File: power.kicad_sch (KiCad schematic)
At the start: 29 parts, among them J7 Conn_01x02, Q1 CSD17311Q5, Q2 CSD17311Q5, U10 DS4432U+, U8 INA260, U9 TPS40305

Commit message: cleanup
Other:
- title: le bitaxeUltra -> BM1366 bitaxe
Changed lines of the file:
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@@
   (paper "A")
   (title_block
-    (title "le bitaxeUltra")
-    (date "2023-07-10")
-    (rev "0")
+    (title "BM1366 bitaxe")
+    (date "2023-10-10")
+    (rev "1.1")
   )
   (junction (at 135.89 116.84) (diameter 0) (color 0 0 0 0)

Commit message: added missing part numbers. updated BOM and iBOM
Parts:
- J7: now left out of the parts list
- U8: DK 296-47777-1-ND -> 296-45218-5-ND; PARTNO INA260AIPWR -> INA260AIPW
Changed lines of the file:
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@@
       (effects (font (size 1.27 1.27)) hide)
     )
-    (property "PARTNO" "INA260AIPWR" (at 67.945 135.89 0)
-      (effects (font (size 1.27 1.27)) hide)
-    )
-    (property "DK" "296-47777-1-ND" (at 67.945 135.89 0)
+    (property "PARTNO" "INA260AIPW" (at 67.945 135.89 0)
+      (effects (font (size 1.27 1.27)) hide)
+    )
+    (property "DK" "296-45218-5-ND" (at 67.945 135.89 0)
       (effects (font (size 1.27 1.27)) hide)
     )
@@
   )
   (symbol (lib_id "Connector_Generic:Conn_01x02") (at 54.102 91.186 0) (unit 1)
-    (in_bom yes) (on_board yes) (dnp no) (fields_autoplaced)
+    (in_bom no) (on_board yes) (dnp no) (fields_autoplaced)
     (property "Reference" "J7" (at 57.15 92.4559 0)
       (effects (font (size 1.27 1.27)) (justify left))

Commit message: adding gerbers
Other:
- note added: "The INA260 is tricky to source. INA260AIPW and INA260AIPWR are both fine. This part is totally optional, feel free to leave it out if you can't source it. If you DNP it, close J7"
- note removed: "The INA260 is currently out of stock everywhere. This part is totally optional, feel free to leave it out if you can't source it. If you DNP it, close J7"
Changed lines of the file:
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@@
     (effects (font (size 1.27 1.27)) (justify left bottom))
   )
-  (text "The INA260 is currently out of stock everywhere.\nThis part is totally optional, feel free to leave \nit out if you can't source it. If you DNP it, close J7"
+  (text "The INA260 is tricky to source. INA260AIPW and INA260AIPWR are both fine.\nThis part is totally optional, feel free to leave \nit out if you can't source it. If you DNP it, close J7"
     (at 45.085 167.005 0)
     (effects (font (size 1.27 1.27)) (justify left bottom))

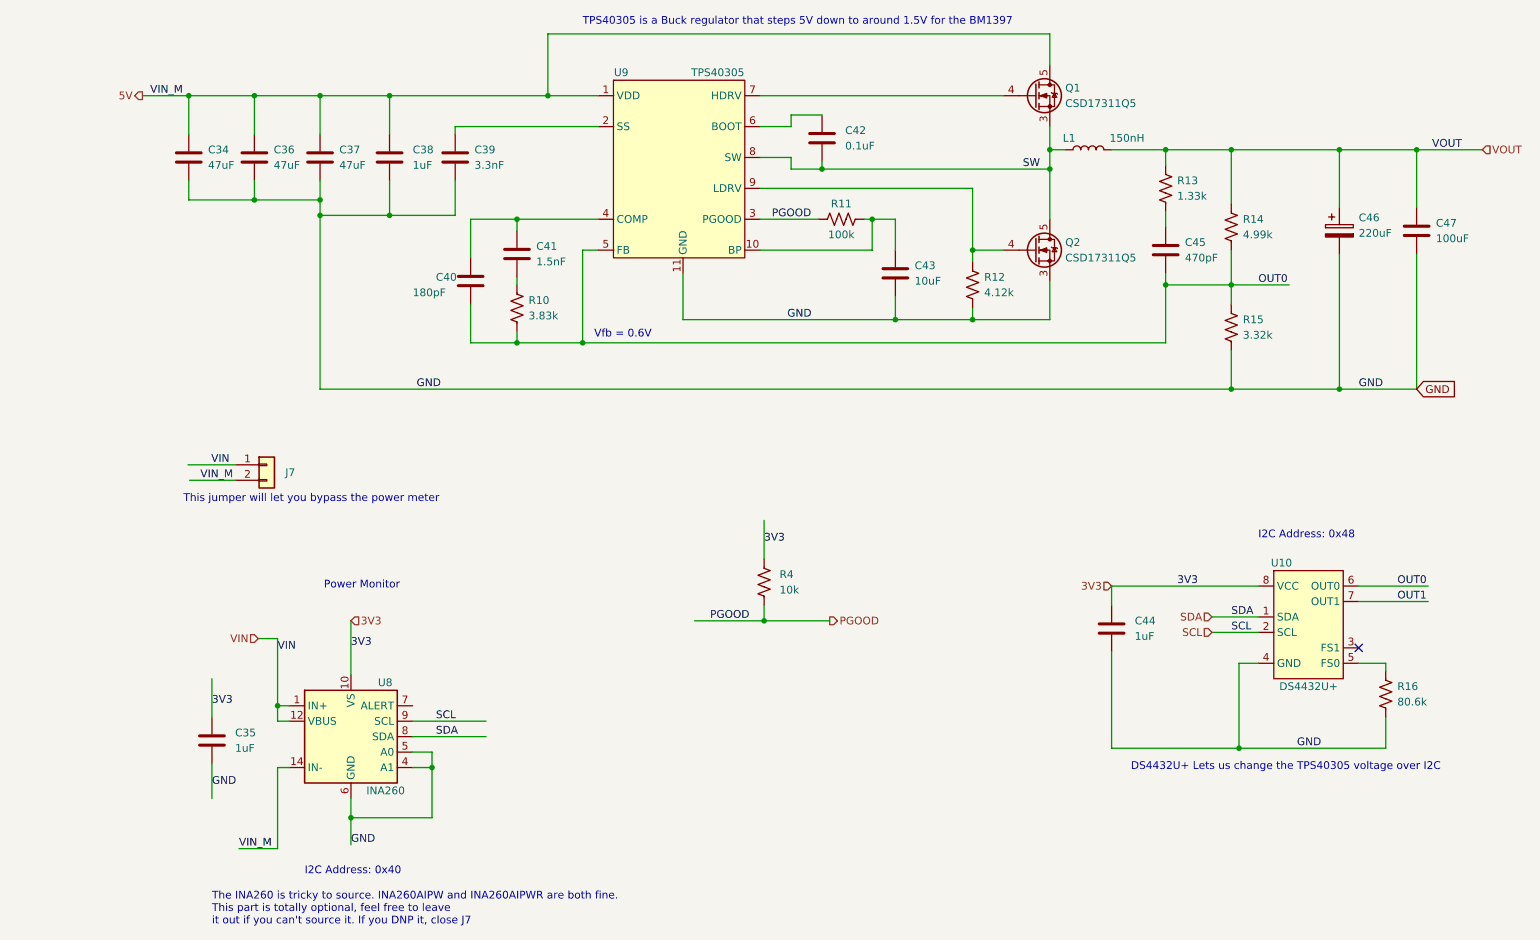
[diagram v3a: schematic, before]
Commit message: added PWR_EN signal to shutdown the TPS40305
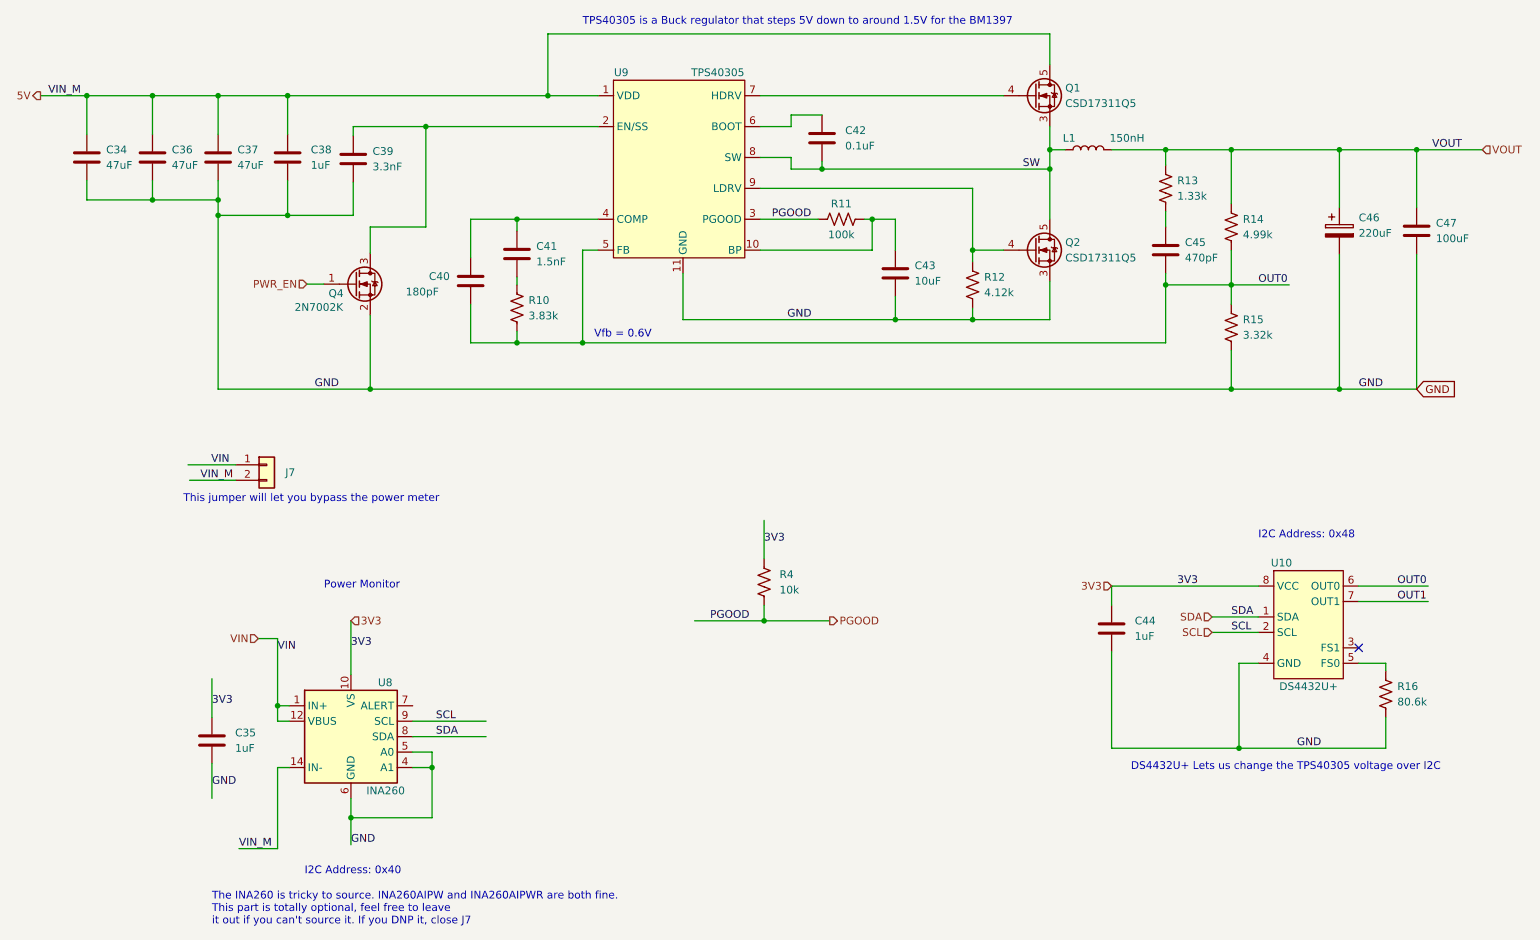
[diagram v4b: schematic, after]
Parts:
- added Q4: 2N7002K, Package_TO_SOT_SMD:SOT-323_SC-70, symbol Transistor_FET:2N7002K
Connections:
- net GND: now also Q4.2 (S)
- net at C39.1, U9.2 (EN/SS): now also Q4.3 (D)
- new net PWR_EN: Q4.1 (G)
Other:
- moved on the sheet: C34, C36, C37, C38, C39

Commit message: misc
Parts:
- R11: now not fitted
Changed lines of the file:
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@@
   )
   (symbol (lib_id "Device:R_US") (at 148.59 50.8 90) (unit 1)
-    (in_bom yes) (on_board yes) (dnp no)
+    (in_bom yes) (on_board yes) (dnp yes)
     (property "Reference" "R11" (at 148.59 48.26 90)
       (effects (font (size 1.27 1.27)))

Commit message: no message
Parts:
- removed R11: 100k, Resistor_SMD:R_0402_1005Metric, symbol Device:R_US
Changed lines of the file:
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@@
   (junction (at 46.101 47.625) (diameter 0) (color 0 0 0 0)
-  )
-  (junction (at 153.67 50.8) (diameter 0) (color 0 0 0 0)
   )
   (junction (at 213.995 137.795) (diameter 0) (color 0 0 0 0)
@@
     (stroke (width 0) (type default))
   )
-  (wire (pts (xy 153.67 55.88) (xy 153.67 50.8))
-    (stroke (width 0) (type default))
-  )
   (wire (pts (xy 230.505 39.37) (xy 230.505 48.895))
     (stroke (width 0) (type default))
@@
     (stroke (width 0) (type default))
   )
-  (wire (pts (xy 135.255 55.88) (xy 153.67 55.88))
+  (wire (pts (xy 135.255 55.88) (xy 157.48 55.88))
     (stroke (width 0) (type default))
   )
@@
     (stroke (width 0) (type default))
   )
-  (wire (pts (xy 152.4 50.8) (xy 153.67 50.8))
-    (stroke (width 0) (type default))
-  )
   (wire (pts (xy 35.306 30.48) (xy 46.101 30.48))
     (stroke (width 0) (type default))
@@
     (stroke (width 0) (type default))
   )
-  (wire (pts (xy 157.48 50.8) (xy 157.48 55.88))
-    (stroke (width 0) (type default))
-  )
   (wire (pts (xy 35.306 30.48) (xy 35.306 36.83))
     (stroke (width 0) (type default))
@@
   )
   (wire (pts (xy 201.93 39.37) (xy 212.725 39.37))
-    (stroke (width 0) (type default))
-  )
-  (wire (pts (xy 153.67 50.8) (xy 157.48 50.8))
     (stroke (width 0) (type default))
   )
@@
     (pin "2")
     (instances
-      (project "bitaxeUltra"
+      (project "bitaxe_RGZ_204_MOD_C"
         (path "/e63e39d7-6ac0-4ffd-8aa3-1841a4541b55/8ec0a9c6-2b78-44ef-a83d-9047d2828409"
           (reference "C43") (unit 1)
@@
     (pin "2")
     (instances
-      (project "bitaxeUltra"
+      (project "bitaxe_RGZ_204_MOD_C"
         (path "/e63e39d7-6ac0-4ffd-8aa3-1841a4541b55/8ec0a9c6-2b78-44ef-a83d-9047d2828409"
           (reference "R14") (unit 1)
@@
     (pin "2")
     (instances
-      (project "bitaxeUltra"
+      (project "bitaxe_RGZ_204_MOD_C"
         (path "/e63e39d7-6ac0-4ffd-8aa3-1841a4541b55/8ec0a9c6-2b78-44ef-a83d-9047d2828409"
           (reference "C37") (unit 1)
@@
     (pin "2")
     (instances
-      (project "bitaxeUltra"
+      (project "bitaxe_RGZ_204_MOD_C"
         (path "/e63e39d7-6ac0-4ffd-8aa3-1841a4541b55/8ec0a9c6-2b78-44ef-a83d-9047d2828409"
           (reference "C46") (unit 1)
@@
     (pin "9")
     (instances
-      (project "bitaxeUltra"
+      (project "bitaxe_RGZ_204_MOD_C"
         (path "/e63e39d7-6ac0-4ffd-8aa3-1841a4541b55/8ec0a9c6-2b78-44ef-a83d-9047d2828409"
           (reference "U9") (unit 1)
@@
     (pin "9")
     (instances
-      (project "bitaxeUltra"
+      (project "bitaxe_RGZ_204_MOD_C"
         (path "/e63e39d7-6ac0-4ffd-8aa3-1841a4541b55/8ec0a9c6-2b78-44ef-a83d-9047d2828409"
           (reference "U8") (unit 1)
@@
     (pin "2")
     (instances
-      (project "bitaxeUltra"
+      (project "bitaxe_RGZ_204_MOD_C"
         (path "/e63e39d7-6ac0-4ffd-8aa3-1841a4541b55/8ec0a9c6-2b78-44ef-a83d-9047d2828409"
           (reference "C34") (unit 1)
@@
     (pin "5")
     (instances
-      (project "bitaxeUltra"
+      (project "bitaxe_RGZ_204_MOD_C"
         (path "/e63e39d7-6ac0-4ffd-8aa3-1841a4541b55/8ec0a9c6-2b78-44ef-a83d-9047d2828409"
           (reference "Q2") (unit 1)
@@
     (pin "2")
     (instances
-      (project "bitaxeUltra"
+      (project "bitaxe_RGZ_204_MOD_C"
         (path "/e63e39d7-6ac0-4ffd-8aa3-1841a4541b55/8ec0a9c6-2b78-44ef-a83d-9047d2828409"
           (reference "C39") (unit 1)
@@
     (pin "2")
     (instances
-      (project "bitaxeUltra"
+      (project "bitaxe_RGZ_204_MOD_C"
         (path "/e63e39d7-6ac0-4ffd-8aa3-1841a4541b55/8ec0a9c6-2b78-44ef-a83d-9047d2828409"
           (reference "C36") (unit 1)
@@
     (pin "2")
     (instances
-      (project "bitaxeUltra"
+      (project "bitaxe_RGZ_204_MOD_C"
         (path "/e63e39d7-6ac0-4ffd-8aa3-1841a4541b55/8ec0a9c6-2b78-44ef-a83d-9047d2828409"
           (reference "C38") (unit 1)
@@
     (pin "8")
     (instances
-      (project "bitaxeUltra"
+      (project "bitaxe_RGZ_204_MOD_C"
         (path "/e63e39d7-6ac0-4ffd-8aa3-1841a4541b55/8ec0a9c6-2b78-44ef-a83d-9047d2828409"
           (reference "U10") (unit 1)
@@
     (pin "2")
     (instances
-      (project "bitaxeUltra"
+      (project "bitaxe_RGZ_204_MOD_C"
         (path "/e63e39d7-6ac0-4ffd-8aa3-1841a4541b55/8ec0a9c6-2b78-44ef-a83d-9047d2828409"
           (reference "C47") (unit 1)
@@
     (pin "2")
     (instances
-      (project "bitaxeUltra"
+      (project "bitaxe_RGZ_204_MOD_C"
         (path "/e63e39d7-6ac0-4ffd-8aa3-1841a4541b55/8ec0a9c6-2b78-44ef-a83d-9047d2828409"
           (reference "C41") (unit 1)
@@
     (pin "2")
     (instances
-      (project "bitaxeUltra"
+      (project "bitaxe_RGZ_204_MOD_C"
         (path "/e63e39d7-6ac0-4ffd-8aa3-1841a4541b55/8ec0a9c6-2b78-44ef-a83d-9047d2828409"
           (reference "R15") (unit 1)
@@
     )
   )
-  (symbol (lib_id "Device:R_US") (at 148.59 50.8 90) (unit 1)
-    (in_bom yes) (on_board yes) (dnp yes)
-    (property "Reference" "R11" (at 148.59 48.26 90)
-      (effects (font (size 1.27 1.27)))
-    )
-    (property "Value" "100k" (at 148.59 53.34 90)
-      (effects (font (size 1.27 1.27)))
-    )
-    (property "Footprint" "Resistor_SMD:R_0402_1005Metric" (at 148.844 49.784 90)
-      (effects (font (size 1.27 1.27)) hide)
-    )
-    (property "Datasheet" "~" (at 148.59 50.8 0)
-      (effects (font (size 1.27 1.27)) hide)
-    )
-    (property "DK" "311-100KJRCT-ND" (at 148.59 50.8 0)
-      (effects (font (size 1.27 1.27)) hide)
-    )
-    (property "PARTNO" "RC0402JR-07100KL" (at 148.59 50.8 0)
-      (effects (font (size 1.27 1.27)) hide)
-    )
-    (pin "1")
-    (pin "2")
-    (instances
-      (project "bitaxeUltra"
-        (path "/e63e39d7-6ac0-4ffd-8aa3-1841a4541b55/8ec0a9c6-2b78-44ef-a83d-9047d2828409"
-          (reference "R11") (unit 1)
-        )
-      )
-    )
-  )
   (symbol (lib_id "Device:C") (at 145.415 37.465 0) (unit 1)
     (in_bom yes) (on_board yes) (dnp no) (fields_autoplaced)
@@
     (pin "2")
     (instances
-      (project "bitaxeUltra"
+      (project "bitaxe_RGZ_204_MOD_C"
         (path "/e63e39d7-6ac0-4ffd-8aa3-1841a4541b55/8ec0a9c6-2b78-44ef-a83d-9047d2828409"
           (reference "C42") (unit 1)
@@
     (pin "3")
     (instances
-      (project "bitaxeUltra"
+      (project "bitaxe_RGZ_204_MOD_C"
         (path "/e63e39d7-6ac0-4ffd-8aa3-1841a4541b55/8ec0a9c6-2b78-44ef-a83d-9047d2828409"
           (reference "Q4") (unit 1)
@@
     (pin "2")
     (instances
-      (project "bitaxeUltra"
+      (project "bitaxe_RGZ_204_MOD_C"
         (path "/e63e39d7-6ac0-4ffd-8aa3-1841a4541b55/8ec0a9c6-2b78-44ef-a83d-9047d2828409"
           (reference "J7") (unit 1)
@@
     (pin "2")
     (instances
-      (project "bitaxeUltra"
+      (project "bitaxe_RGZ_204_MOD_C"
         (path "/e63e39d7-6ac0-4ffd-8aa3-1841a4541b55/8ec0a9c6-2b78-44ef-a83d-9047d2828409"
           (reference "R16") (unit 1)
@@
     (pin "2")
     (instances
-      (project "bitaxeUltra"
+      (project "bitaxe_RGZ_204_MOD_C"
         (path "/e63e39d7-6ac0-4ffd-8aa3-1841a4541b55/8ec0a9c6-2b78-44ef-a83d-9047d2828409"
           (reference "C44") (unit 1)
@@
     (pin "2")
     (instances
-      (project "bitaxeUltra"
+      (project "bitaxe_RGZ_204_MOD_C"
         (path "/e63e39d7-6ac0-4ffd-8aa3-1841a4541b55/8ec0a9c6-2b78-44ef-a83d-9047d2828409"
           (reference "R13") (unit 1)
@@
     (pin "2")
     (instances
-      (project "bitaxeUltra"
+      (project "bitaxe_RGZ_204_MOD_C"
         (path "/e63e39d7-6ac0-4ffd-8aa3-1841a4541b55/8ec0a9c6-2b78-44ef-a83d-9047d2828409"
           (reference "R10") (unit 1)
@@
     (pin "5")
     (instances
-      (project "bitaxeUltra"
+      (project "bitaxe_RGZ_204_MOD_C"
         (path "/e63e39d7-6ac0-4ffd-8aa3-1841a4541b55/8ec0a9c6-2b78-44ef-a83d-9047d2828409"
           (reference "Q1") (unit 1)
@@
     (pin "2")
     (instances
-      (project "bitaxeUltra"
+      (project "bitaxe_RGZ_204_MOD_C"
         (path "/e63e39d7-6ac0-4ffd-8aa3-1841a4541b55/8ec0a9c6-2b78-44ef-a83d-9047d2828409"
           (reference "C45") (unit 1)
@@
     (pin "2")
     (instances
-      (project "bitaxeUltra"
+      (project "bitaxe_RGZ_204_MOD_C"
         (path "/e63e39d7-6ac0-4ffd-8aa3-1841a4541b55/8ec0a9c6-2b78-44ef-a83d-9047d2828409"
           (reference "L1") (unit 1)
@@
     (pin "2")
     (instances
-      (project "bitaxeUltra"
+      (project "bitaxe_RGZ_204_MOD_C"
         (path "/e63e39d7-6ac0-4ffd-8aa3-1841a4541b55/8ec0a9c6-2b78-44ef-a83d-9047d2828409"
           (reference "R12") (unit 1)
@@
     (pin "2")
     (instances
-      (project "bitaxeUltra"
+      (project "bitaxe_RGZ_204_MOD_C"
         (path "/e63e39d7-6ac0-4ffd-8aa3-1841a4541b55/8ec0a9c6-2b78-44ef-a83d-9047d2828409"
           (reference "C35") (unit 1)
@@
     (pin "2")
     (instances
-      (project "bitaxeUltra"
+      (project "bitaxe_RGZ_204_MOD_C"
         (path "/e63e39d7-6ac0-4ffd-8aa3-1841a4541b55/8ec0a9c6-2b78-44ef-a83d-9047d2828409"
           (reference "C40") (unit 1)
@@
     (pin "2")
     (instances
-      (project "bitaxeUltra"
+      (project "bitaxe_RGZ_204_MOD_C"
         (path "/e63e39d7-6ac0-4ffd-8aa3-1841a4541b55/8ec0a9c6-2b78-44ef-a83d-9047d2828409"
           (reference "R4") (unit 1)
